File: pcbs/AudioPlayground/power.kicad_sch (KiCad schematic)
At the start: 23 parts, among them U10 MCP73831-2-OT, U11 74LVC1GU04DRL, U12 AP2280, U13 74CBTLV3245, U5 XC6209F332MR, U6 XC6209F182MR, U9 LM66200DRLR

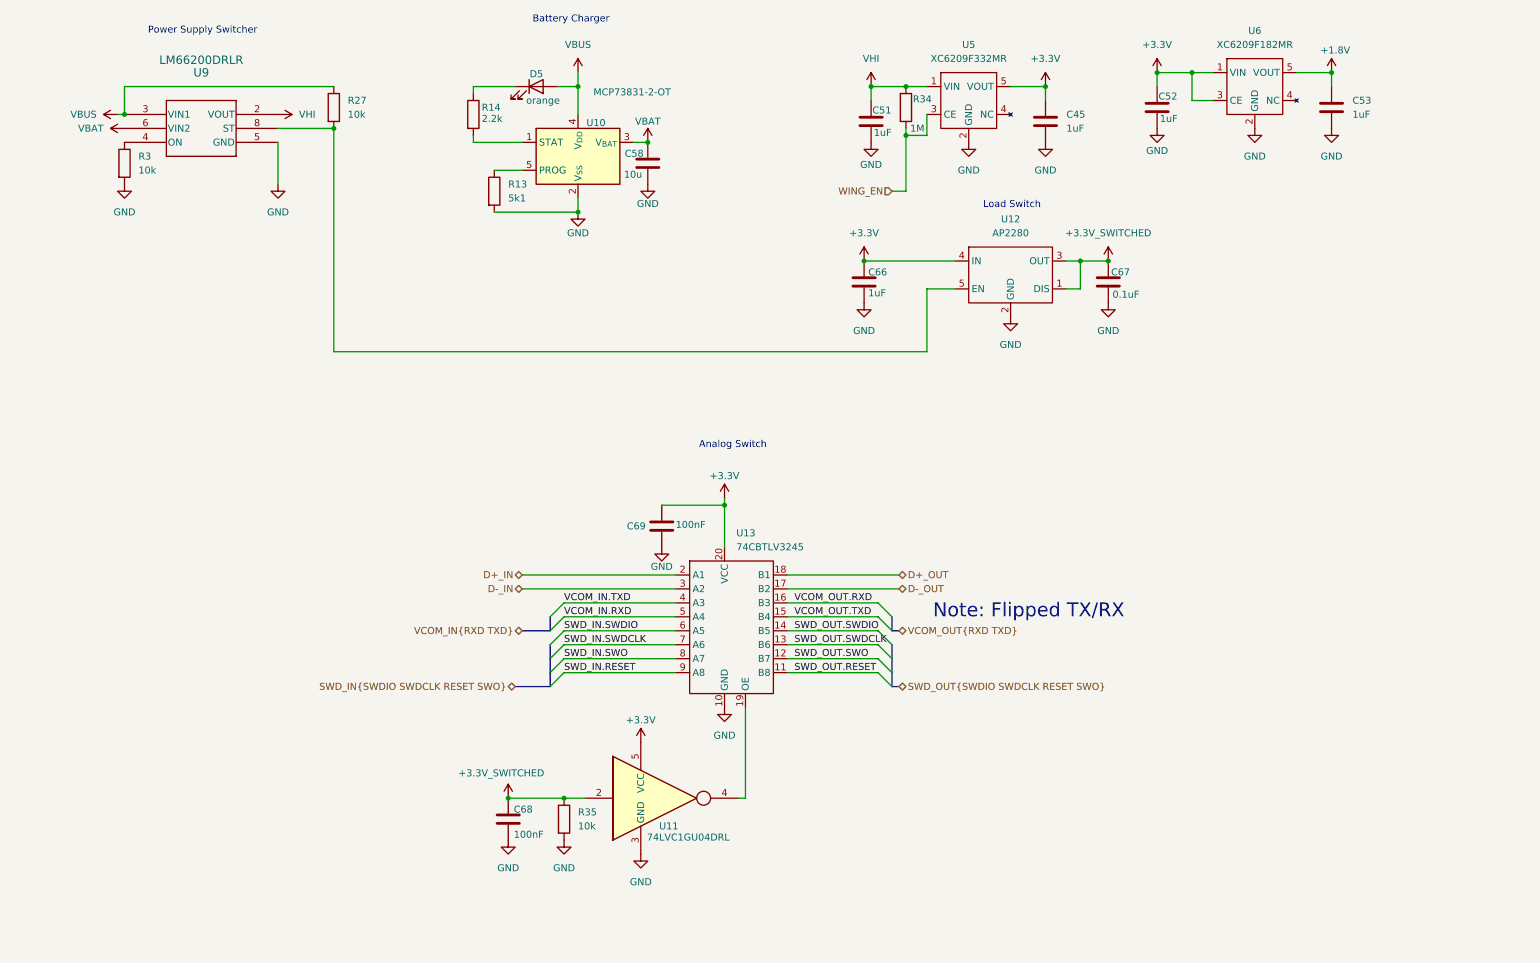
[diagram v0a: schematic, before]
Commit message: added usb221, removed usb connections from bus-switch.
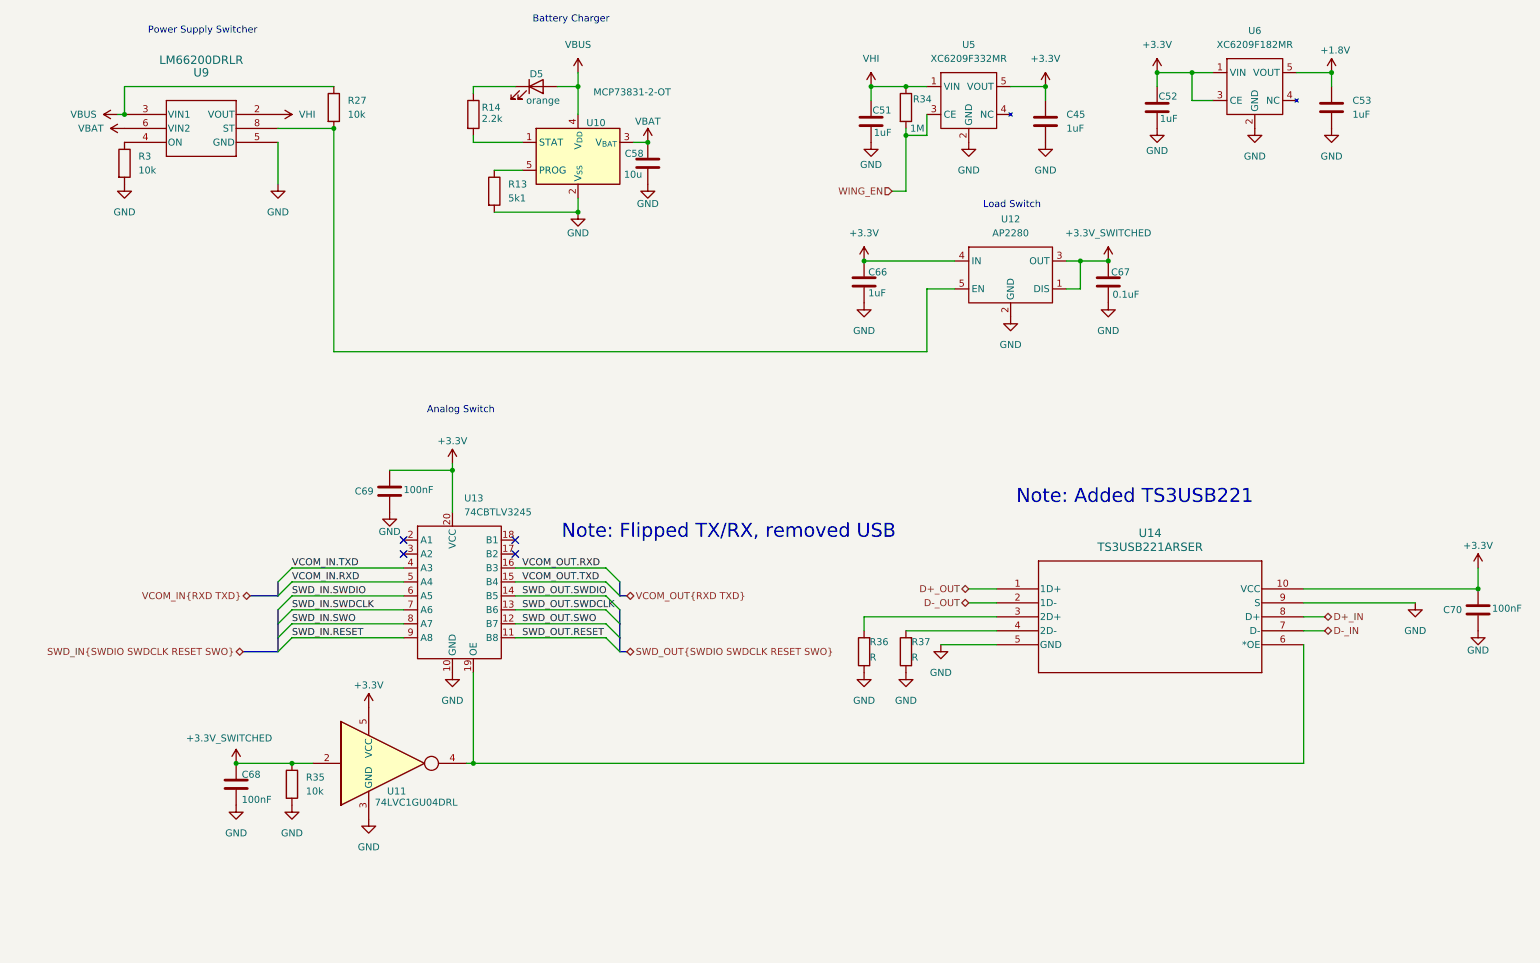
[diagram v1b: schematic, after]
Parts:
- added C70: 100nF, Capacitor_SMD:C_0402_1005Metric, symbol Device:C
- added R36, R37: R, Resistor_SMD:R_0402_1005Metric, symbol Device:R
- added U14: TS3USB221ARSER, TS3USB221A:TS3USB221A, symbol TS3USB221A:TS3USB221A
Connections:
- net +3.3V: now also C70.1, U14.10 (VCC)
- net D+_IN: now also U14.8 (D+); no longer U13.2 (A1)
- net D+_OUT: now also U14.1 (1D+); no longer U13.18 (B1)
- net D-_IN: now also U14.7 (D-); no longer U13.3 (A2)
- net D-_OUT: now also U14.2 (1D-); no longer U13.17 (B2)
- net GND: now also C70.2, R36.1, R37.1, U14.5 (GND), U14.9 (S)
- net at U11.4, U13.19 (OE): now also U14.6 (*OE)
- new net: R36.2, U14.3 (2D+)
- new net: R37.2, U14.4 (2D-)
- no-connect marks 0 -> 4
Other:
- note added: "Note: Added TS3USB221"
- note added: "Note: Flipped TX/RX, removed USB"
- note removed: "Note: Flipped TX/RX"
- moved on the sheet: C68, C69, R35, U11, U13

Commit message: Add LCSC and fix RF
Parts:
- C45, C51, C52, C53, C66: LCSC (none) -> C52923
- C58: value 10u -> 10uF; LCSC (none) -> C15525
- C67: value 0.1uF -> 100nF; LCSC (none) -> C1525
- C68, C69, C70: LCSC (none) -> C1525
- D5: LCSC (none) -> C88330
- R13: LCSC (none) -> C25905
- R14: LCSC (none) -> C25879
- R27, R3, R35: LCSC (none) -> C25744
- R34: LCSC (none) -> C26083
- R36, R37: value R -> 27R; now not fitted; now left out of the parts list
- U10: LCSC (none) -> C382138
- U12: LCSC (none) -> C128637
- U14: LCSC (none) -> C128396
- U5: LCSC (none) -> C216624
- U6: LCSC (none) -> C236671
- U9: LCSC (none) -> C3235556
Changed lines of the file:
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@@
 			)
 		)
+		(property "LCSC" "C26083"
+			(at 170.18 35.56 0)
+			(effects
+				(font
+					(size 1.27 1.27)
+				)
+				(hide yes)
+			)
+		)
 		(pin "2"
 		)
@@
 			)
 		)
+		(property "LCSC" "C52923"
+			(at 195.58 38.1 0)
+			(effects
+				(font
+					(size 1.27 1.27)
+				)
+				(hide yes)
+			)
+		)
 		(pin "2"
 		)
@@
 			)
 		)
+		(property "LCSC" "C25744"
+			(at 58.42 158.75 0)
+			(effects
+				(font
+					(size 1.27 1.27)
+				)
+				(hide yes)
+			)
+		)
 		(pin "1"
 		)
@@
 			)
 		)
+		(property "LCSC" "C52923"
+			(at 247.65 35.56 0)
+			(effects
+				(font
+					(size 1.27 1.27)
+				)
+				(hide yes)
+			)
+		)
 		(pin "2"
 		)
@@
 			)
 		)
+		(property "LCSC" "C52923"
+			(at 215.9 35.56 0)
+			(effects
+				(font
+					(size 1.27 1.27)
+				)
+				(hide yes)
+			)
+		)
 		(pin "2"
 		)
@@
 			)
 		)
-		(property "Value" "0.1uF"
+		(property "Value" "100nF"
 			(at 207.772 69.596 0)
 			(effects
@@
 			)
 		)
+		(property "LCSC" "C1525"
+			(at 207.01 67.31 0)
+			(effects
+				(font
+					(size 1.27 1.27)
+				)
+				(hide yes)
+			)
+		)
 		(pin "2"
 		)
@@
 			)
 		)
-		(property "Value" "10u"
-			(at 122.174 47.752 0)
+		(property "Value" "10uF"
+			(at 122.936 47.752 0)
 			(effects
 				(font
@@
 			)
 		)
+		(property "LCSC" "C15525"
+			(at 123.19 45.72 0)
+			(effects
+				(font
+					(size 1.27 1.27)
+				)
+				(hide yes)
+			)
+		)
 		(pin "2"
 		)
@@
 			)
 		)
+		(property "LCSC" "C216624"
+			(at 181.61 34.29 0)
+			(effects
+				(font
+					(size 1.27 1.27)
+				)
+				(hide yes)
+			)
+		)
 		(pin "1"
 		)
@@
 			)
 		)
+		(property "LCSC" "C88330"
+			(at 102.87 31.75 0)
+			(effects
+				(font
+					(size 1.27 1.27)
+				)
+				(hide yes)
+			)
+		)
 		(pin "2"
 		)
@@
 			)
 		)
+		(property "LCSC" "C128396"
+			(at 186.69 123.19 0)
+			(effects
+				(font
+					(size 1.27 1.27)
+				)
+				(hide yes)
+			)
+		)
 		(pin "6"
 		)
@@
 			)
 		)
+		(property "LCSC" "C25905"
+			(at 95.25 50.8 0)
+			(effects
+				(font
+					(size 1.27 1.27)
+				)
+				(hide yes)
+			)
+		)
 		(pin "1"
 		)
@@
 			)
 		)
+		(property "LCSC" "C25744"
+			(at 66.04 35.56 0)
+			(effects
+				(font
+					(size 1.27 1.27)
+				)
+				(hide yes)
+			)
+		)
 		(pin "1"
 		)
@@
 			)
 		)
+		(property "LCSC" "C3235556"
+			(at 41.91 41.91 0)
+			(effects
+				(font
+					(size 1.27 1.27)
+				)
+				(hide yes)
+			)
+		)
 		(pin "4"
 		)
@@
 			)
 		)
+		(property "LCSC" "C25879"
+			(at 91.44 36.83 0)
+			(effects
+				(font
+					(size 1.27 1.27)
+				)
+				(hide yes)
+			)
+		)
 		(pin "1"
 		)
@@
 			)
 		)
+		(property "LCSC" "C52923"
+			(at 163.83 38.1 0)
+			(effects
+				(font
+					(size 1.27 1.27)
+				)
+				(hide yes)
+			)
+		)
 		(pin "2"
 		)
@@
 			)
 		)
+		(property "LCSC" "C1525"
+			(at 274.32 127 0)
+			(effects
+				(font
+					(size 1.27 1.27)
+				)
+				(hide yes)
+			)
+		)
 		(pin "2"
 		)
@@
 		(unit 1)
 		(exclude_from_sim no)
-		(in_bom yes)
+		(in_bom no)
 		(on_board yes)
-		(dnp no)
+		(dnp yes)
 		(property "Reference" "R36"
 			(at 163.576 132.842 0)
@@
 			)
 		)
-		(property "Value" "R"
+		(property "Value" "27R"
 			(at 163.576 135.636 0)
 			(effects
@@
 			)
 		)
+		(property "LCSC" "C1525"
+			(at 76.2 105.41 0)
+			(effects
+				(font
+					(size 1.27 1.27)
+				)
+				(hide yes)
+			)
+		)
 		(pin "2"
 		)
@@
 			)
 		)
+		(property "LCSC" "C128637"
+			(at 189.23 67.31 0)
+			(effects
+				(font
+					(size 1.27 1.27)
+				)
+				(hide yes)
+			)
+		)
 		(pin "4"
 		)
@@
 			)
 		)
+		(property "LCSC" "C25744"
+			(at 27.94 45.72 0)
+			(effects
+				(font
+					(size 1.27 1.27)
+				)
+				(hide yes)
+			)
+		)
 		(pin "1"
 		)
@@
 			)
 		)
+		(property "LCSC" "C1525"
+			(at 48.26 158.75 0)
+			(effects
+				(font
+					(size 1.27 1.27)
+				)
+				(hide yes)
+			)
+		)
 		(pin "1"
 		)
@@
 			)
 		)
+		(property "LCSC" "C52923"
+			(at 162.56 67.31 0)
+			(effects
+				(font
+					(size 1.27 1.27)
+				)
+				(hide yes)
+			)
+		)
 		(pin "2"
 		)
@@
 			)
 		)
+		(property "LCSC" "C382138"
+			(at 110.49 44.45 0)
+			(effects
+				(font
+					(size 1.27 1.27)
+				)
+				(hide yes)
+			)
+		)
 		(pin "4"
 		)
@@
 			)
 		)
+		(property "LCSC" "C236671"
+			(at 233.68 31.75 0)
+			(effects
+				(font
+					(size 1.27 1.27)
+				)
+				(hide yes)
+			)
+		)
 		(pin "1"
 		)
@@
 		(unit 1)
 		(exclude_from_sim no)
-		(in_bom yes)
+		(in_bom no)
 		(on_board yes)
-		(dnp no)
+		(dnp yes)
 		(property "Reference" "R37"
 			(at 171.196 132.842 0)
@@
 			)
 		)
-		(property "Value" "R"
+		(property "Value" "27R"
 			(at 171.196 135.636 0)
 			(effects

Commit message: Fix values
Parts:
- R13: value 5k1 -> 5.1k
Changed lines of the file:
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@@
 			)
 		)
-		(property "Value" "5k1"
+		(property "Value" "5.1k"
 			(at 97.79 52.0699 0)
 			(effects

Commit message: Update MICs
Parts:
- removed C68, C69: 100nF, Capacitor_SMD:C_0402_1005Metric, symbol Device:C
- removed R35: 10k, Resistor_SMD:R_0402_1005Metric, symbol Device:R
- removed R36, R37: 27R, Resistor_SMD:R_0402_1005Metric, symbol Device:R
- removed U11: 74LVC1GU04DRL, Package_TO_SOT_SMD:SOT-553, symbol 74xGxx:74LVC1GU04DRL
- removed U13: 74CBTLV3245, Package_DFN_QFN:DHVQFN-20-1EP_2.5x4.5mm_P0.5mm_EP1x3mm, symbol 74CBTLV3245:74CBTLV3245
- added U11, U13, U16, U17, U18: SN74LVC1G126DRYR(UMW), SN74LVC1G126DRYR:SN74LVC1G126DRYR, symbol SN74LVC1G126DRYR:SN74LVC1G126DRYR(UMW)
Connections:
- net +3.3V: now also U11.6 (VCC), U13.6 (VCC), U16.6 (VCC), U17.6 (VCC), U18.6 (VCC)
- net +3.3V_SWITCHED: now also U14.9 (S), U11.1 (OE), U13.1 (OE), U16.1 (OE), U17.1 (OE), U18.1 (OE)
- net D+_OUT: now also U14.3 (2D+); no longer U14.1 (1D+)
- net D-_OUT: now also U14.4 (2D-); no longer U14.2 (1D-)
- net GND: now also U14.6 (*OE), U11.3 (GND), U13.3 (GND), U16.3 (GND), U17.3 (GND), U18.3 (GND); no longer U14.9 (S)
- net SWD_IN.RESET: now also U18.2 (INA)
- net SWD_IN.SWDCLK: now also U17.2 (INA)
- net SWD_IN.SWDIO: now also U16.2 (INA)
- net SWD_OUT.RESET: now also U18.4 (Y)
- net SWD_OUT.SWDCLK: now also U17.4 (Y)
- net SWD_OUT.SWDIO: now also U16.4 (Y)
- net VCOM_IN.RXD: now also U13.2 (INA)
- net VCOM_IN.TXD: now also U11.2 (INA)
- net VCOM_OUT.RXD: now also U11.4 (Y)
- net VCOM_OUT.TXD: now also U13.4 (Y)
- net ST: now reaches R27.2, U12.5 (EN), U9.8 (ST)
- no-connect marks 4 -> 7
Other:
- note added: "Analog Switches"
- note added: "Note: Flipped TX/RX"
- note removed: "Analog Switch"
- note removed: "Note: Added TS3USB221"
- note removed: "Note: Flipped TX/RX, removed USB"
- moved on the sheet: C70, R27

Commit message: Change Analog Switches
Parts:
- removed U11, U13, U16, U17, U18: SN74LVC1G126DRYR(UMW), SN74LVC1G126DRYR:SN74LVC1G126DRYR, symbol SN74LVC1G126DRYR:SN74LVC1G126DRYR(UMW)
- added U11, U13, U16, U17, U21: SN74LVC1G66DRYR, C507245:SN74LVC1G66DRYR, symbol SN74LVC1G66DRYR:SN74LVC1G66DRYR
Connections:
- net +3.3V: now also U11.6 (VCC), U13.6 (VCC), U16.6 (VCC), U17.6 (VCC), U21.6 (VCC)
- net +3.3V_SWITCHED: now also U11.4 (C), U13.4 (C), U16.4 (C), U17.4 (C), U21.4 (C)
- net GND: now also U11.3 (GND), U13.3 (GND), U16.3 (GND), U17.3 (GND), U21.3 (GND)
- net SWD_IN.RESET: now also U17.1 (A)
- net SWD_IN.SWDCLK: now also U16.1 (A)
- net SWD_IN.SWDIO: now also U13.1 (A)
- net SWD_OUT.RESET: now also U17.2 (B)
- net SWD_OUT.SWDCLK: now also U16.2 (B)
- net SWD_OUT.SWDIO: now also U13.2 (B)
- net VCOM_IN.RXD: now also U11.1 (A)
- net VCOM_IN.TXD: now also U21.1 (A)
- net VCOM_OUT.RXD: now also U21.2 (B)
- net VCOM_OUT.TXD: now also U11.2 (B)

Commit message: V2.1
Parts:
- added TP10: TX, TestPoint:TestPoint_Pad_D1.0mm, symbol Connector:TestPoint
- added TP11: RX, TestPoint:TestPoint_Pad_D1.0mm, symbol Connector:TestPoint
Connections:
- net VCOM_OUT.RXD: now also TP11.1
- net VCOM_OUT.TXD: now also TP10.1
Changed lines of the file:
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@@
+	)
+	(symbol
+		(lib_id "Connector:TestPoint")
+		(at 31.75 107.95 90)
+		(unit 1)
+		(exclude_from_sim no)
+		(in_bom no)
+		(on_board yes)
+		(dnp no)
+		(fields_autoplaced yes)
+		(property "Reference" "TP10"
+			(at 28.448 102.87 90)
+			(effects
+				(font
+					(size 1.27 1.27)
+				)
+			)
+		)
+		(property "Value" "TX"
+			(at 28.448 105.41 90)
+			(effects
+				(font
+					(size 1.27 1.27)
+				)
+			)
+		)
+		(property "Footprint" "TestPoint:TestPoint_Pad_D1.0mm"
+			(at 31.75 102.87 0)
+			(effects
+				(font
+					(size 1.27 1.27)
+				)
+				(hide yes)
+			)
+		)
+		(property "Datasheet" "~"
+			(at 31.75 102.87 0)
+			(effects
+				(font
+					(size 1.27 1.27)
+				)
+				(hide yes)
+			)
+		)
+		(property "Description" "test point"
+			(at 31.75 107.95 0)
+			(effects
+				(font
+					(size 1.27 1.27)
+				)
+				(hide yes)
+			)
+		)
+		(pin "1"
+		)
+		(instances
+			(project "AudioPlayground"
+				(path "/1c455b59-0247-4883-9aca-444b4cb10447/00e8f514-2643-4d38-960e-87a1e0dce405"
+					(reference "TP10")
+					(unit 1)
+				)
+			)
+		)
 	)
 	(symbol
@@
 					(unit 1)
 				)
+			)
+		)
+	)
+	(symbol
+		(lib_id "Connector:TestPoint")
+		(at 31.75 87.63 90)
+		(unit 1)
+		(exclude_from_sim no)
+		(in_bom no)
+		(on_board yes)
+		(dnp no)
+		(fields_autoplaced yes)
+		(property "Reference" "TP11"
+			(at 28.448 82.55 90)
+			(effects
+				(font
+					(size 1.27 1.27)
+				)
+			)
+		)
+		(property "Value" "RX"
+			(at 28.448 85.09 90)
+			(effects
+				(font
+					(size 1.27 1.27)
+				)
+			)
+		)
+		(property "Footprint" "TestPoint:TestPoint_Pad_D1.0mm"
+			(at 31.75 82.55 0)
+			(effects
+				(font
+					(size 1.27 1.27)
+				)
+				(hide yes)
+			)
+		)
+		(property "Datasheet" "~"
+			(at 31.75 82.55 0)
+			(effects
+				(font
+					(size 1.27 1.27)
+				)
+				(hide yes)
+			)
+		)
+		(property "Description" "test point"
+			(at 31.75 87.63 0)
+			(effects
+				(font
+					(size 1.27 1.27)
+				)
+				(hide yes)
+			)
+		)
+		(pin "1"
+		)
+		(instances
+			(project "AudioPlayground"
+				(path "/1c455b59-0247-4883-9aca-444b4cb10447/00e8f514-2643-4d38-960e-87a1e0dce405"
+					(reference "TP11")
+					(unit 1)
+				)

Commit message: Improve Optic
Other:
- note removed: "Note: Flipped TX/RX"
- title: (none) -> LE Audio Playground
- moved on the sheet: C45, C51, C52, C53, C58, C66, C67, C70, D5, R13, R14, R27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
